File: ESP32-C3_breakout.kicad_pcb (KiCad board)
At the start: 2 copper layers, 45.7 x 21.3 mm, 32 parts, among them J1 USB4105-GF-A, J2 Conn_01x11_Male, J3 Conn_01x11_Male, SW1 SW_Push, SW2 SW_Push, U1 LD1117S33TR_SOT223, U2 ESP32-C3, Y1 40MHz

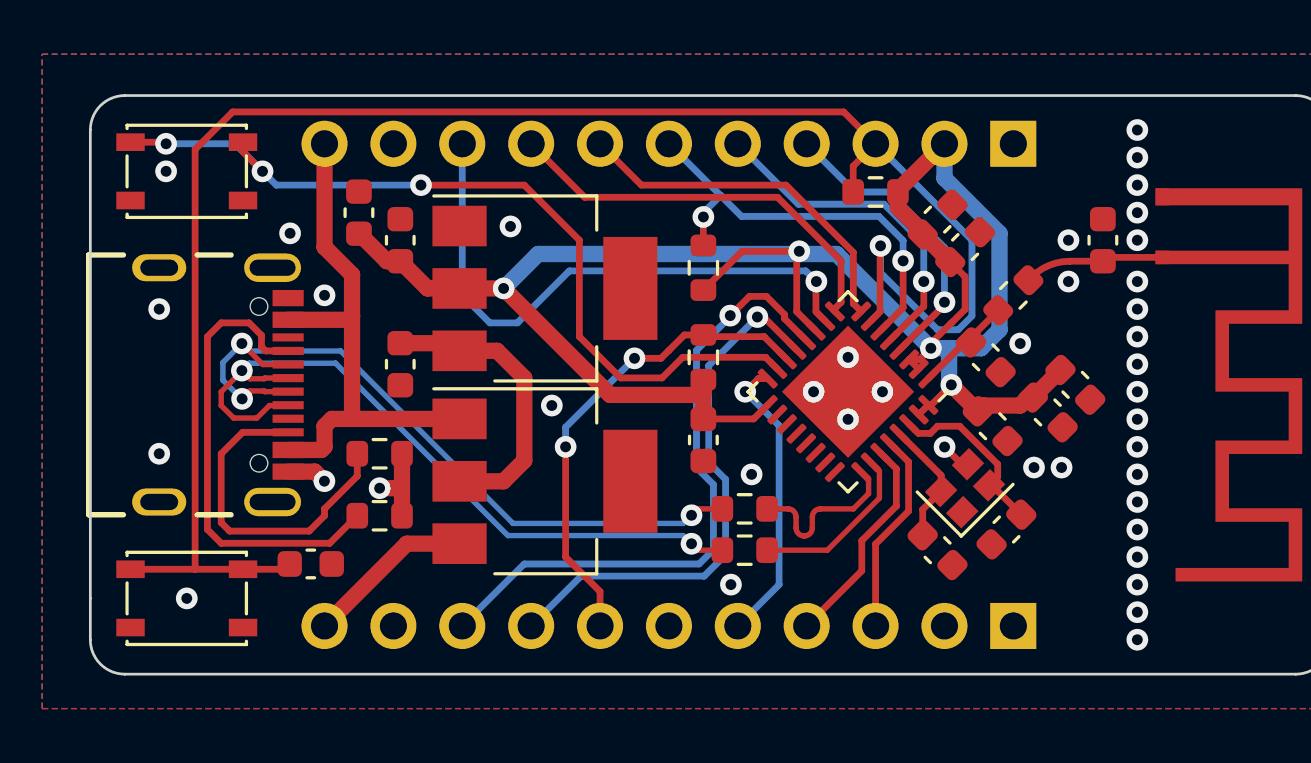
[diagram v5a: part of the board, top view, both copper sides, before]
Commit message: Differential pair routing change
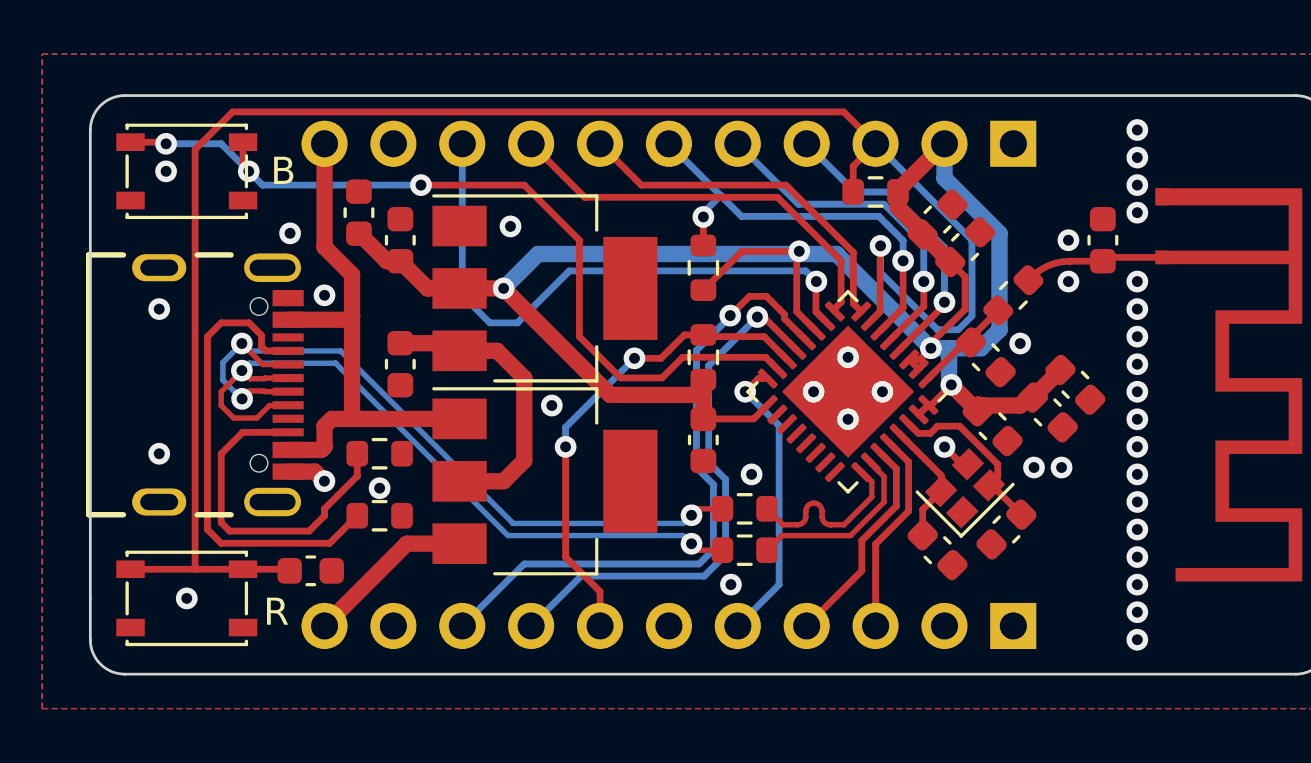
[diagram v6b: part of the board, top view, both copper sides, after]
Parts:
- moved C1 0.25 mm to (158.5, 78.7)
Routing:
- net GND: track 5.71 -> 2.61 mm, vias 41 -> 40
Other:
- board text added: "B"
- board text added: "R"
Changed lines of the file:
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@@
   )
   (footprint "Capacitor_SMD:C_0603_1608Metric" (layer "F.Cu")
-    (at 158.496 78.486)
+    (at 158.496 78.74)
     (descr "Capacitor SMD 0603 (1608 Metric), square (rectangular) end terminal, IPC_7351 nominal, (Body size source: IPC-SM-782 page 76, https://www.pcb-3d.com/wordpress/wp-content/uploads/ipc-sm-782a_amendment_1_and_2.pdf), generated with kicad-footprint-generator")
     (tags "capacitor")
@@
     (effects (font (size 1 1) (thickness 0.15)) (justify left mirror))
   )
+  (gr_text "R\n" (at 157.226 80.264) (layer "F.SilkS")
+    (effects (font (size 1 1) (thickness 0.15)))
+  )
+  (gr_text "B\n" (at 157.48 64.008) (layer "F.SilkS")
+    (effects (font (size 1 1) (thickness 0.15)))
+  )
   (segment (start 181.742117 75.216564) (end 180.208349 73.682796) (width 0.25) (layer "F.Cu") (net 1))
   (segment (start 181.061992 76.478191) (end 181.061992 77.429992) (width 0.25) (layer "F.Cu") (net 1))
   (segment (start 181.061992 76.478191) (end 181.742117 75.798066) (width 0.25) (layer "F.Cu") (net 1))
   (segment (start 181.742117 75.798066) (end 181.742117 75.216564) (width 0.25) (layer "F.Cu") (net 1))
-  (segment (start 161.036 75.692) (end 161.798 75.692) (width 0.6) (layer "F.Cu") (net 2))
-  (segment (start 161.861 75.629) (end 161.798 75.692) (width 0.6) (layer "F.Cu") (net 2))
-  (segment (start 161.861 75.755) (end 161.861 76.708) (width 0.6) (layer "F.Cu") (net 2))
-  (segment (start 161.798 75.692) (end 161.861 75.755) (width 0.6) (layer "F.Cu") (net 2))
-  (segment (start 161.861 74.422) (end 161.861 75.629) (width 0.6) (layer "F.Cu") (net 2))
   (segment (start 182.504117 74.808117) (end 181.868299 74.172299) (width 0.25) (layer "F.Cu") (net 2))
   (segment (start 158.648 75.082) (end 158.999701 75.433701) (width 0.6) (layer "F.Cu") (net 2))
@@
   (via (at 188.976 73.152) (size 0.8) (drill 0.4) (layers "F.Cu" "B.Cu") (free) (net 2))
   (via (at 188.976 75.184) (size 0.8) (drill 0.4) (layers "F.Cu" "B.Cu") (free) (net 2))
-  (via (at 188.976 66.548) (size 0.8) (drill 0.4) (layers "F.Cu" "B.Cu") (free) (net 2))
   (via (at 188.976 74.168) (size 0.8) (drill 0.4) (layers "F.Cu" "B.Cu") (free) (net 2))
   (via (at 188.976 77.216) (size 0.8) (drill 0.4) (layers "F.Cu" "B.Cu") (free) (net 2))
@@
   (segment (start 155.50648 77.27448) (end 155.194 76.962) (width 0.25) (layer "F.Cu") (net 17))
   (segment (start 155.194 76.962) (end 155.194 74.422) (width 0.25) (layer "F.Cu") (net 17))
-  (segment (start 176.092 76.454) (end 175.323 76.454) (width 0.2) (layer "F.Cu") (net 19))
-  (segment (start 176.392 77.154) (end 176.392 76.754) (width 0.2) (layer "F.Cu") (net 19))
-  (segment (start 178.504994 76.454) (end 177.292 76.454) (width 0.2) (layer "F.Cu") (net 19))
-  (segment (start 179.065995 75.892999) (end 178.504994 76.454) (width 0.2) (layer "F.Cu") (net 19))
-  (segment (start 179.065995 75.368869) (end 179.065995 75.892999) (width 0.2) (layer "F.Cu") (net 19))
-  (segment (start 178.794136 75.09701) (end 179.065995 75.368869) (width 0.2) (layer "F.Cu") (net 19))
-  (segment (start 176.992 76.754) (end 176.992 77.154) (width 0.2) (layer "F.Cu") (net 19))
-  (arc (start 176.992 77.154) (mid 176.904132 77.366132) (end 176.692 77.454) (width 0.2) (layer "F.Cu") (net 19))
-  (arc (start 177.292 76.454) (mid 177.079868 76.541868) (end 176.992 76.754) (width 0.2) (layer "F.Cu") (net 19))
-  (arc (start 176.692 77.454) (mid 176.479868 77.366132) (end 176.392 77.154) (width 0.2) (layer "F.Cu") (net 19))
-  (arc (start 176.392 76.754) (mid 176.304132 76.541868) (end 176.092 76.454) (width 0.2) (layer "F.Cu") (net 19))
-  (segment (start 179.465515 76.058485) (end 177.546 77.978) (width 0.2) (layer "F.Cu") (net 20))
-  (segment (start 179.465515 75.061282) (end 179.465515 76.058485) (width 0.2) (layer "F.Cu") (net 20))
-  (segment (start 179.147689 74.743456) (end 179.465515 75.061282) (width 0.2) (layer "F.Cu") (net 20))
-  (segment (start 177.546 77.978) (end 175.323 77.978) (width 0.2) (layer "F.Cu") (net 20))
+  (segment (start 175.323 76.454) (end 175.910481 77.041481) (width 0.2) (layer "F.Cu") (net 19))
+  (segment (start 178.82949 75.09701) (end 178.794136 75.09701) (width 0.2) (layer "F.Cu") (net 19))
+  (segment (start 177.700519 77.041481) (end 178.164319 77.041481) (width 0.2) (layer "F.Cu") (net 19))
+  (segment (start 176.750519 76.741481) (end 176.750519 76.545648) (width 0.2) (layer "F.Cu") (net 19))
+  (segment (start 178.164319 77.041481) (end 179.185755 76.020045) (width 0.2) (layer "F.Cu") (net 19))
+  (segment (start 177.650519 77.041481) (end 177.700519 77.041481) (width 0.2) (layer "F.Cu") (net 19))
+  (segment (start 177.350519 76.545648) (end 177.350519 76.741481) (width 0.2) (layer "F.Cu") (net 19))
+  (segment (start 179.185755 76.020045) (end 179.185755 75.453275) (width 0.2) (layer "F.Cu") (net 19))
+  (segment (start 179.185755 75.453275) (end 178.82949 75.09701) (width 0.2) (layer "F.Cu") (net 19))
+  (segment (start 175.910481 77.041481) (end 176.450519 77.041481) (width 0.2) (layer "F.Cu") (net 19))
+  (arc (start 176.450519 77.041481) (mid 176.662651 76.953613) (end 176.750519 76.741481) (width 0.2) (layer "F.Cu") (net 19))
+  (arc (start 176.750519 76.545648) (mid 176.838387 76.333516) (end 177.050519 76.245648) (width 0.2) (layer "F.Cu") (net 19))
+  (arc (start 177.350519 76.741481) (mid 177.438387 76.953613) (end 177.650519 77.041481) (width 0.2) (layer "F.Cu") (net 19))
+  (arc (start 177.050519 76.245648) (mid 177.262651 76.333516) (end 177.350519 76.545648) (width 0.2) (layer "F.Cu") (net 19))
+  (segment (start 179.147689 74.743456) (end 179.147689 74.778811) (width 0.2) (layer "F.Cu") (net 20))
+  (segment (start 178.401199 77.441001) (end 175.859999 77.441001) (width 0.2) (layer "F.Cu") (net 20))
+  (segment (start 179.147689 74.778811) (end 179.635755 75.266877) (width 0.2) (layer "F.Cu") (net 20))
+  (segment (start 179.635755 75.266877) (end 179.635755 76.206445) (width 0.2) (layer "F.Cu") (net 20))
+  (segment (start 179.635755 76.206445) (end 178.401199 77.441001) (width 0.2) (layer "F.Cu") (net 20))
+  (segment (start 175.859999 77.441001) (end 175.323 77.978) (width 0.2) (layer "F.Cu") (net 20))
   (segment (start 179.147689 69.528544) (end 179.490514 69.185719) (width 0.25) (layer "F.Cu") (net 21))
   (segment (start 179.490514 69.185719) (end 179.490514 66.773426) (width 0.25) (layer "F.Cu") (net 21))
@@
   (segment (start 175.270233 70.866) (end 175.700544 71.296311) (width 0.25) (layer "F.Cu") (net 22))
   (segment (start 151.849 62.933) (end 153.103 62.933) (width 0.25) (layer "F.Cu") (net 22))
-  (segment (start 156.718 64.008) (end 155.999 63.289) (width 0.25) (layer "F.Cu") (net 22))
-  (segment (start 155.999 63.289) (end 155.999 62.933) (width 0.25) (layer "F.Cu") (net 22))
   (segment (start 166.37 64.516) (end 168.402 66.548) (width 0.25) (layer "F.Cu") (net 22))
   (segment (start 169.926 71.628) (end 171.45 71.628) (width 0.25) (layer "F.Cu") (net 22))
   (segment (start 168.402 70.104) (end 169.926 71.628) (width 0.25) (layer "F.Cu") (net 22))
+  (segment (start 155.999 62.933) (end 155.999 63.797) (width 0.25) (layer "F.Cu") (net 22))
   (segment (start 166.37 64.516) (end 162.56 64.516) (width 0.25) (layer "F.Cu") (net 22))
   (segment (start 171.45 71.628) (end 172.212 70.866) (width 0.25) (layer "F.Cu") (net 22))
+  (segment (start 155.999 63.797) (end 156.21 64.008) (width 0.25) (layer "F.Cu") (net 22))
   (segment (start 172.212 70.866) (end 175.270233 70.866) (width 0.25) (layer "F.Cu") (net 22))
   (via (at 162.56 64.516) (size 0.8) (drill 0.4) (layers "F.Cu" "B.Cu") (net 22))
-  (via (at 156.718 64.008) (size 0.8) (drill 0.4) (layers "F.Cu" "B.Cu") (net 22))
   (via (at 153.162 62.992) (size 0.8) (drill 0.4) (layers "F.Cu" "B.Cu") (net 22))
-  (segment (start 157.226 64.516) (end 156.718 64.008) (width 0.25) (layer "B.Cu") (net 22))
-  (segment (start 153.162 62.992) (end 155.702 62.992) (width 0.25) (layer "B.Cu") (net 22))
-  (segment (start 162.56 64.516) (end 157.226 64.516) (width 0.25) (layer "B.Cu") (net 22))
-  (segment (start 155.702 62.992) (end 156.718 64.008) (width 0.25) (layer "B.Cu") (net 22))
+  (via (at 156.21 64.008) (size 0.8) (drill 0.4) (layers "F.Cu" "B.Cu") (net 22))
+  (segment (start 155.194 62.992) (end 154.686 62.992) (width 0.25) (layer "B.Cu") (net 22))
+  (segment (start 156.718 64.516) (end 162.56 64.516) (width 0.25) (layer "B.Cu") (net 22))
+  (segment (start 153.162 62.992) (end 154.686 62.992) (width 0.25) (layer "B.Cu") (net 22))
+  (segment (start 156.21 64.008) (end 155.194 62.992) (width 0.25) (layer "B.Cu") (net 22))
+  (segment (start 156.21 64.008) (end 156.718 64.516) (width 0.25) (layer "B.Cu") (net 22))
   (segment (start 180.208349 70.589204) (end 181.864 68.933553) (width 0.25) (layer "F.Cu") (net 23))
   (segment (start 181.864 68.933553) (end 181.864 68.834) (width 0.25) (layer "F.Cu") (net 23))
@@
   (segment (start 156.256 72.107) (end 156.775499 72.107) (width 0.2) (layer "F.Cu") (net 36))
   (segment (start 172.774002 76.454) (end 172.537002 76.691) (width 0.2) (layer "F.Cu") (net 36))
-  (segment (start 155.956 72.407) (end 155.9645 72.3985) (width 0.2) (layer "F.Cu") (net 36))
   (via (at 155.956 70.357497) (size 0.8) (drill 0.4) (layers "F.Cu" "B.Cu") (net 36))
   (via (at 155.9645 72.3985) (size 0.8) (drill 0.4) (layers "F.Cu" "B.Cu") (net 36))

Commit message: Minor improvements
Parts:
- C11: renamed from C14; value C -> 3.9 pF
- C12: renamed from C13; value C -> 5.3pF
- D1: value C4D10120D -> BAT120C
- L1: value L -> 1.8 nH
- R2: renamed from R7; value 10k -> 22R
- R3: renamed from R6; value 10k -> 22R
- renumbered C10 to C1, C9 to C10, C7 to C13, C8 to C14, C11 to C2, C12 to C3, C1 to C4, C2 to C5, C3 to C6, C4 to C7, C5 to C8, C6 to C9, R2 to R6, R3 to R7
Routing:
- net GND: vias 40 -> 41

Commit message: General improvements
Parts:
- removed AE1: Antenna, ESP_Antenna:ESPRESSIF_ESP32_MIFA_2.4GHz_Right
- removed the R2 at (174.5, 78.0)
- removed the R3 at (174.5, 76.5)
- added AE2: Antenna_Shield, ESP_Antenna:ESPRESSIF_ESP32_MIFA_2.4GHz_Right, F.Cu at (190.0, 67.3)
- added IC1: STF202-22T1G, Package_SO:TSOP-6_1.65x3.05mm_P0.95mm, F.Cu at (174.5, 77.2)
- moved C7 0.36 mm to (182.9, 67.1)
- moved C9 0.25 mm to (186.7, 71.6)
- moved C12 0.18 mm to (183.3, 70.7)
- moved C11 0.13 mm to (187.7, 66.4)
- renumbered R4 to R2, R5 to R3, R6 to R4, R7 to R5
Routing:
- net /USB_+5V: track 20.2 -> 36.6 mm, vias 0 -> 2
- net /EN: track 66.3 -> 55.5 mm, vias 1 -> 0
- net +3V3: track 75.0 -> 77.3 mm
- net GND: track 2.61 -> 3.65 mm, vias 41 -> 66
- net /GPIO7: track 20.0 -> 21.0 mm
- net /GPIO6: track 23.7 -> 24.6 mm
